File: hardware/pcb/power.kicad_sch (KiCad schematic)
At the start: 53 parts, among them U1 AXP209, U2 SY8008, U3 NX3P1108UK, U4 NX3P1108UK, U5 NX3P1108UK, U6 NX3P1108UK, U7 ADP121-1.2

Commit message: - Working on pcb layout
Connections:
- net PMU_VBUSEN: no longer names the net of U1.6 (~VBUSEN)
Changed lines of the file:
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@@
-    (stroke (width 0) (type solid) (color 0 0 0 0))
-  )
-  (wire (pts (xy 116.84 162.56) (xy 114.3 162.56))
     (stroke (width 0) (type solid) (color 0 0 0 0))
   )
@@
     (effects (font (size 1.27 1.27)) (justify right))
     (property "Intersheet References" "${INTERSHEET_REFS}" (id 0) (at 43.18 27.94 0)
-      (effects (font (size 1.27 1.27)) hide)
-    )
-  )
-  (global_label "PMU_VBUSEN" (shape input) (at 114.3 162.56 180)
-    (effects (font (size 1.27 1.27)) (justify right))
-    (property "Intersheet References" "${INTERSHEET_REFS}" (id 0) (at 43.18 27.94 0)

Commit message: - PCB r0.3 routed, need to finalize
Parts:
- removed C24, C25: 10uF, Capacitor_SMD:C_0402_1005Metric, symbol Device:C
- removed C27: 1uF, Capacitor_SMD:C_0402_1005Metric, symbol Device:C
- removed L4: 4.7uH, Inductor_SMD:L_1008_2520Metric, symbol Device:L
- removed R6: 200K, Resistor_SMD:R_0402_1005Metric, symbol Device:R
- removed R7: 100K, Resistor_SMD:R_0402_1005Metric, symbol Device:R
- removed U2: SY8008, Package_TO_SOT_SMD:TSOT-23-5, symbol symbols:SY8008
- removed U4: NX3P1108UK, Package_CSP:WLCSP-4-X1-WLB0909-4_0.89x0.89mm_P0.5mm, symbol symbols:NX3P1108UK
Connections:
- net +1V8: now also C15.2, C16.2, L3.2, U1.17 (DCDC3)
- net +3V3: now also C20.2, U1.12 (LDO2); no longer C15.2, C16.2, L3.2, U1.17 (DCDC3)
- net GND: now also U1.29 (DC3SET)
- net IPSOUT: no longer U1.29 (DC3SET)
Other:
- moved on the sheet: C28, R8, U5

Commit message: - PCB layout finished for r0p3
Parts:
- U3, U5, U6: footprint Package_CSP:WLCSP-4-X1-WLB0909-4_0.89x0.89mm_P0.5mm -> footprint:CSP-4_2x2_1.0x1.0mm
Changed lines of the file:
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@@
     (property "Reference" "U3" (id 0) (at 223.52 93.98 0))
     (property "Value" "NX3P1108UK" (id 1) (at 223.52 96.52 0))
-    (property "Footprint" "Package_CSP:WLCSP-4-X1-WLB0909-4_0.89x0.89mm_P0.5mm" (id 2) (at 223.52 93.98 0)
+    (property "Footprint" "footprint:CSP-4_2x2_1.0x1.0mm" (id 2) (at 223.52 93.98 0)
       (effects (font (size 1.27 1.27)) hide)
     )
@@
     (property "Reference" "U5" (id 0) (at 223.52 114.3 0))
     (property "Value" "NX3P1108UK" (id 1) (at 223.52 116.84 0))
-    (property "Footprint" "Package_CSP:WLCSP-4-X1-WLB0909-4_0.89x0.89mm_P0.5mm" (id 2) (at 223.52 114.3 0)
+    (property "Footprint" "footprint:CSP-4_2x2_1.0x1.0mm" (id 2) (at 223.52 114.3 0)
       (effects (font (size 1.27 1.27)) hide)
     )
@@
     (property "Reference" "U6" (id 0) (at 294.64 93.98 0))
     (property "Value" "NX3P1108UK" (id 1) (at 294.64 96.52 0))
-    (property "Footprint" "Package_CSP:WLCSP-4-X1-WLB0909-4_0.89x0.89mm_P0.5mm" (id 2) (at 294.64 93.98 0)
+    (property "Footprint" "footprint:CSP-4_2x2_1.0x1.0mm" (id 2) (at 294.64 93.98 0)
       (effects (font (size 1.27 1.27)) hide)
     )

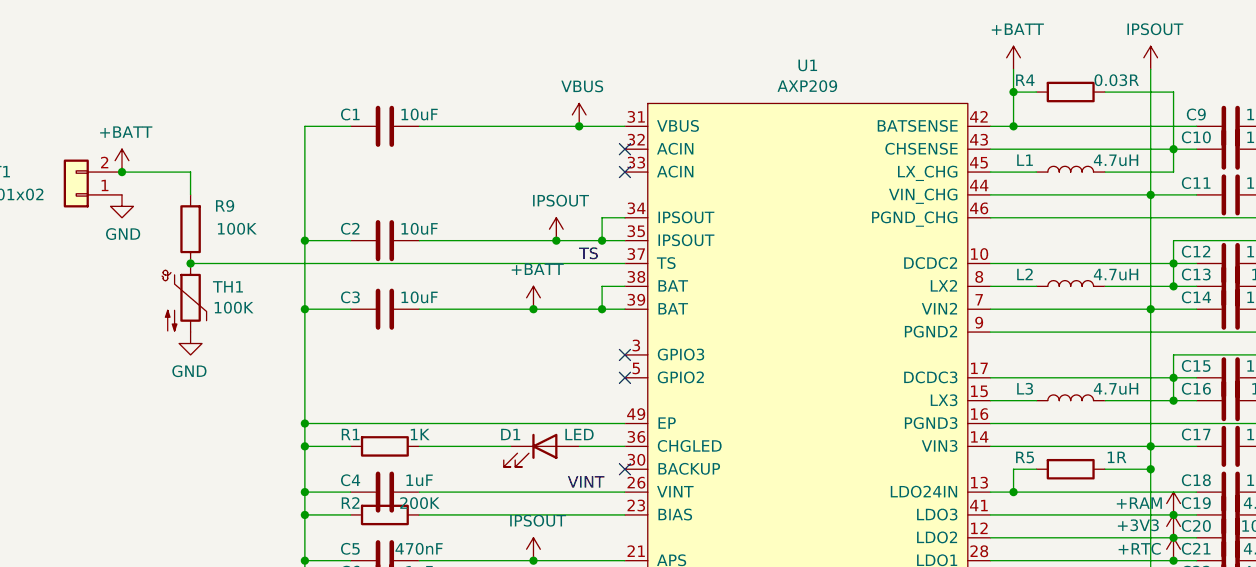
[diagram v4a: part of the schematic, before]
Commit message: - pcb: r0p4, update to KiCAD 6.0
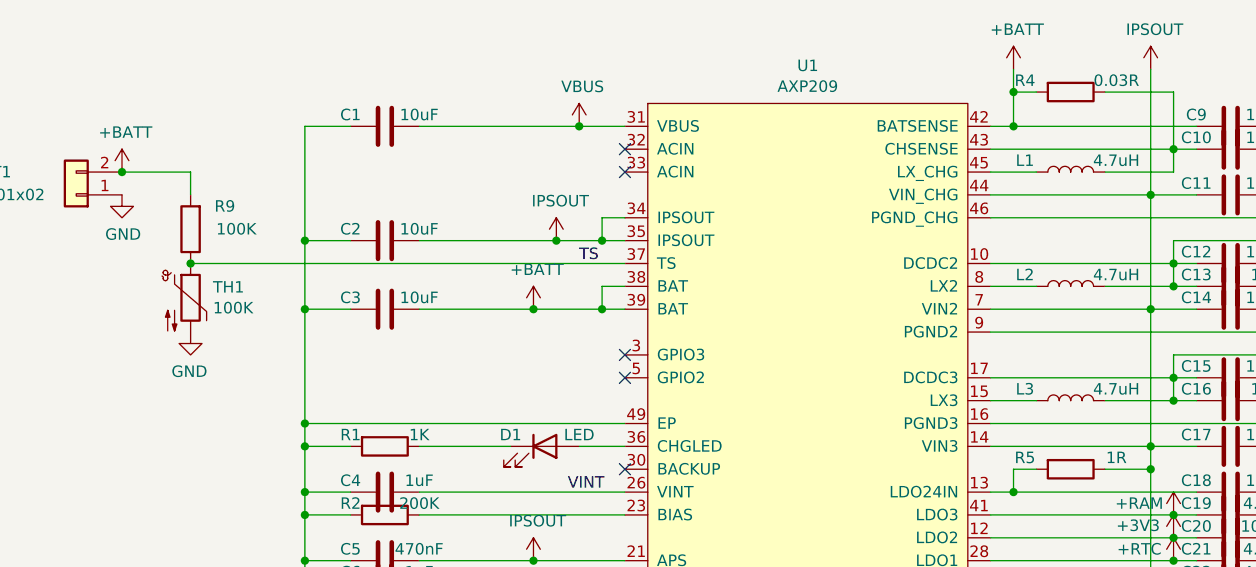
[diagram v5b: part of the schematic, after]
